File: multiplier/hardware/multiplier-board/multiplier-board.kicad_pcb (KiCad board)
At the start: 2 copper layers, 76.2 x 134.1 mm, 80 parts, among them U1 74AHCT08, U10 74HCT688, U11 74AHCT08, U12 74AHCT08, U13 74AHCT08, U14 74AHCT08, U15 74AHCT08, U16 74AHCT08, U17 74AHCT08, U18 74AHCT08, U19 ATF16V10C, U2 74AHCT08, U20 74AHCT374, U21 74LS283, U22 74LS283, U23 74LS283, U24 74LS283, U25 74LS283, U26 74LS283, U27 74LS283, U28 74AHCT374, U29 74LS283, U3 74AHCT08, U30 74LS283, U31 74LS283, U32 74LS283, U33 74LS283, U34 74LS283, U35 74LS283, U36 74AHCT245, U37 74AHCT245, U4 74AHCT08, U5 74AHCT08, U6 74AHCT08, U7 74AHCT08, U8 74AHCT08, U9 74HCT688

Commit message: corrected part designator
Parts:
- U21, U22, U23, U24, U25, U26, U27, U29, U30, U31, U32, U33, U34, U35: value 74LS283 -> 74HCT283
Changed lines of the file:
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@@
 			)
 		)
-		(property "Value" "74LS283"
+		(property "Value" "74HCT283"
 			(at 0 5.9 90)
 			(layer "F.Fab")
@@
 			)
 		)
-		(property "Value" "74LS283"
+		(property "Value" "74HCT283"
 			(at 0 5.9 90)
 			(layer "F.Fab")
@@
 			)
 		)
-		(property "Value" "74LS283"
+		(property "Value" "74HCT283"
 			(at 0 5.9 90)
 			(layer "F.Fab")
@@
 			)
 		)
-		(property "Value" "74LS283"
+		(property "Value" "74HCT283"
 			(at 0 5.9 90)
 			(layer "F.Fab")
@@
 			)
 		)
-		(property "Value" "74LS283"
+		(property "Value" "74HCT283"
 			(at 0 5.9 90)
 			(layer "F.Fab")
@@
 			)
 		)
-		(property "Value" "74LS283"
+		(property "Value" "74HCT283"
 			(at 0 5.9 90)
 			(layer "F.Fab")
@@
 			)
 		)
-		(property "Value" "74LS283"
+		(property "Value" "74HCT283"
 			(at 0 5.9 90)
 			(layer "F.Fab")
@@
 			)
 		)
-		(property "Value" "74LS283"
+		(property "Value" "74HCT283"
 			(at 0 5.9 90)
 			(layer "F.Fab")
@@
 			)
 		)
-		(property "Value" "74LS283"
+		(property "Value" "74HCT283"
 			(at 0 5.9 90)
 			(layer "F.Fab")
@@
 			)
 		)
-		(property "Value" "74LS283"
+		(property "Value" "74HCT283"
 			(at 0 5.9 90)
 			(layer "F.Fab")
@@
 			)
 		)
-		(property "Value" "74LS283"
+		(property "Value" "74HCT283"
 			(at 0 5.9 90)
 			(layer "F.Fab")
@@
 			)
 		)
-		(property "Value" "74LS283"
+		(property "Value" "74HCT283"
 			(at 0 5.9 90)
 			(layer "F.Fab")
@@
 			)
 		)
-		(property "Value" "74LS283"
+		(property "Value" "74HCT283"
 			(at 0 5.9 90)
 			(layer "F.Fab")
@@
 			)
 		)
-		(property "Value" "74LS283"
+		(property "Value" "74HCT283"
 			(at 0 5.9 90)
 			(layer "F.Fab")

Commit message: update kicad version
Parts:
- U19: value ATF16V10C -> ATF16V8C
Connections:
- net Net-(U19-I5) renamed /ADDR_HIGH
- net Net-(U20-Cp) renamed /AIN
- net Net-(U28-Cp) renamed /BIN
- net Net-(U36-CE) renamed /RHIGH
- net Net-(U37-CE) renamed /RLOW

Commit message: corrected issues
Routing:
- net CLK: track 27.7 -> 44.8 mm
- net GND: track 1248.2 -> 1235.3 mm
- net +5V: track 782.5 -> 791.8 mm
- net ~{RO}: track 62.0 -> 66.9 mm
- net /BUS4: track 100.3 -> 104.0 mm
- net /BUS6: track 93.5 -> 97.3 mm
- net /ADDR8: track 46.1 -> 49.7 mm
- net /ADDR10: track 34.2 -> 37.8 mm
- net /BUS2: track 108.2 -> 111.8 mm
- net /ADDR6: track 22.0 -> 25.5 mm
- net /BUS0: track 94.8 -> 98.4 mm
- net /ADDR4: track 20.9 -> 24.4 mm
- net /ADDR13: track 33.5 -> 30.0 mm
- net /ADDR15: track 34.2 -> 30.7 mm
- net /ADDR1: track 23.7 -> 20.2 mm
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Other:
- board text added: "v1.1 by Michael Kanmprath"
- board text removed: "v1.0 by Michael Kanmprath"

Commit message: changed pcb to 4-layer with internal ground planes
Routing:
- net GND: track 1235.3 -> 1241.5 mm
- added copper zone on In1.Cu, net GND
- added copper zone on In2.Cu, net GND
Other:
- copper layers 2 -> 4
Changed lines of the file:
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@@
 	(layers
 		(0 "F.Cu" signal)
+		(4 "In1.Cu" signal)
+		(6 "In2.Cu" signal)
 		(2 "B.Cu" signal)
 		(9 "F.Adhes" user "F.Adhesive")
@@
 	)
 	(setup
+		(stackup
+			(layer "F.SilkS"
+				(type "Top Silk Screen")
+			)
+			(layer "F.Paste"
+				(type "Top Solder Paste")
+			)
+			(layer "F.Mask"
+				(type "Top Solder Mask")
+				(thickness 0.01)
+			)
+			(layer "F.Cu"
+				(type "copper")
+				(thickness 0.035)
+			)
+			(layer "dielectric 1"
+				(type "prepreg")
+				(thickness 0.1)
+				(material "FR4")
+				(epsilon_r 4.5)
+				(loss_tangent 0.02)
+			)
+			(layer "In1.Cu"
+				(type "copper")
+				(thickness 0.035)
+			)
+			(layer "dielectric 2"
+				(type "core")
+				(thickness 1.24)
+				(material "FR4")
+				(epsilon_r 4.5)
+				(loss_tangent 0.02)
+			)
+			(layer "In2.Cu"
+				(type "copper")
+				(thickness 0.035)
+			)
+			(layer "dielectric 3"
+				(type "prepreg")
+				(thickness 0.1)
+				(material "FR4")
+				(epsilon_r 4.5)
+				(loss_tangent 0.02)
+			)
+			(layer "B.Cu"
+				(type "copper")
+				(thickness 0.035)
+			)
+			(layer "B.Mask"
+				(type "Bottom Solder Mask")
+				(thickness 0.01)
+			)
+			(layer "B.Paste"
+				(type "Bottom Solder Paste")
+			)
+			(layer "B.SilkS"
+				(type "Bottom Silk Screen")
+			)
+			(copper_finish "None")
+			(dielectric_constraints no)
+		)
 		(pad_to_mask_clearance 0)
 		(allow_soldermask_bridges_in_footprints no)
@@
 	)
 	(segment
+		(start 106.9 147.56)
+		(end 106.9 147.4)
+		(width 0.75)
+		(layer "In1.Cu")
+		(net 2)
+	)
+	(segment
+		(start 106.9 147.4)
+		(end 105 145.5)
+		(width 0.75)
+		(layer "In1.Cu")
+		(net 2)
+	)
+	(segment
+		(start 106.9 147.56)
+		(end 105 145.66)
+		(width 0.75)
+		(layer "In2.Cu")
+		(net 2)
+	)
+	(segment
+		(start 105 145.66)
+		(end 105 145)
+		(width 0.75)
+		(layer "In2.Cu")
+		(net 2)
+	)
+	(segment
 		(start 110.824 144.769169)
 		(end 110.824 146.404)
@@
 		(net 2)
 		(net_name "GND")
-		(layer "B.Cu")
+		(layers "B.Cu" "In1.Cu" "In2.Cu")
 		(hatch edge 0.5)
 		(connect_pads

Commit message: improved signal line isolation
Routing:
- net /AIN: track 47.8 -> 54.1 mm
- net /BIN: track 50.6 -> 52.8 mm
- net GND: track 1241.5 -> 1239.7 mm
- net /RLOW: track 63.6 -> 62.6 mm, vias 1 -> 2
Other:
- board text added: "v1.2 by Michael Kanmprath"
- board text removed: "v1.1 by Michael Kanmprath"
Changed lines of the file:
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@@
 		(layer "Edge.Cuts")
 	)
-	(gr_text "v1.1 by Michael Kanmprath"
+	(gr_text "v1.2 by Michael Kanmprath"
 		(at 159.131 19.6342 270)
 		(layer "F.SilkS")
@@
 	)
 	(segment
+		(start 91.868 98.0694)
+		(end 91.868 93.6752)
+		(width 0.75)
+		(layer "B.Cu")
+		(net 2)
+	)
+	(segment
 		(start 152.146 137.6934)
 		(end 158.0134 137.6934)
@@
 	)
 	(segment
-		(start 91.8718 98.024348)
-		(end 96.220948 93.6752)
-		(width 0.75)
-		(layer "B.Cu")
-		(net 2)
-	)
-	(segment
 		(start 146.9644 142.875)
 		(end 152.146 137.6934)
@@
 	)
 	(segment
-		(start 96.220948 93.6752)
-		(end 125.984 93.6752)
-		(width 0.75)
-		(layer "B.Cu")
-		(net 2)
-	)
-	(segment
 		(start 103.632 18.796)
 		(end 104.775 19.939)
@@
 	)
 	(segment
-		(start 91.868 98.0694)
+		(start 91.868 93.6752)
 		(end 91.868 20.5415)
 		(width 0.75)
@@
 	)
 	(segment
-		(start 125.984 93.6752)
-		(end 128.4732 96.1644)
-		(width 0.75)
-		(layer "B.Cu")
-		(net 2)
-	)
-	(segment
 		(start 122.301 18.796)
 		(end 138.049 18.796)
@@
 	)
 	(segment
+		(start 128.4732 96.1644)
+		(end 125.984 93.6752)
+		(width 0.75)
+		(layer "B.Cu")
+		(net 2)
+	)
+	(segment
 		(start 118.6688 129.3915)
 		(end 121.7129 129.3915)
@@
 	)
 	(segment
+		(start 125.984 93.6752)
+		(end 91.868 93.6752)
+		(width 0.75)
+		(layer "B.Cu")
+		(net 2)
+	)
+	(segment
 		(start 104.902 20.066)
 		(end 105.156 20.32)
@@
 	)
 	(segment
-		(start 95.3262 102.8954)
-		(end 95.3262 95.8596)
+		(start 107.823 123.9012)
+		(end 107.2642 123.3424)
 		(width 0.2)
 		(layer "B.Cu")
@@
 	)
 	(segment
-		(start 100.4824 108.0516)
-		(end 95.3262 102.8954)
+		(start 107.2642 111.2012)
+		(end 105.0544 108.9914)
 		(width 0.2)
 		(layer "B.Cu")
@@
 	)
 	(segment
-		(start 95.3262 95.8596)
-		(end 95.3008 95.8342)
+		(start 116.1288 123.3932)
+		(end 115.6208 123.9012)
 		(width 0.2)
 		(layer "B.Cu")
@@
 	)
 	(segment
-		(start 105.41 108.0516)
-		(end 100.4824 108.0516)
+		(start 105.0544 108.9914)
+		(end 94.2848 108.9914)
 		(width 0.2)
 		(layer "B.Cu")
@@
 	)
 	(segment
-		(start 107.2388 122.936)
-		(end 107.2388 109.8804)
+		(start 116.1288 121.7715)
+		(end 116.1288 123.3932)
 		(width 0.2)
 		(layer "B.Cu")
@@
 	)
 	(segment
-		(start 108.6358 124.333)
-		(end 107.2388 122.936)
+		(start 92.964 107.6706)
+		(end 92.964 96.5454)
 		(width 0.2)
 		(layer "B.Cu")
@@
 	)
 	(segment
-		(start 107.2388 109.8804)
-		(end 105.41 108.0516)
+		(start 92.964 96.5454)
+		(end 93.6752 95.8342)
 		(width 0.2)
 		(layer "B.Cu")
@@
 	)
 	(segment
-		(start 116.1288 121.7715)
-		(end 116.1288 123.1646)
+		(start 115.6208 123.9012)
+		(end 107.823 123.9012)
+		(width 0.2)
+		(layer "B.Cu")
+		(net 112)
+	)
+	(segment
+		(start 94.2848 108.9914)
+		(end 92.964 107.6706)
+		(width 0.2)
+		(layer "B.Cu")
+		(net 112)
+	)
+	(segment
+		(start 107.2642 123.3424)
+		(end 107.2642 111.2012)
 		(width 0.2)
 		(layer "B.Cu")
@@
 	)
 	(segment
-		(start 116.1288 123.1646)
-		(end 114.9604 124.333)
+		(start 95.3262 95.8596)
+		(end 95.3008 95.8342)
 		(width 0.2)
 		(layer "B.Cu")
@@
 	)
 	(segment
-		(start 114.9604 124.333)
-		(end 108.6358 124.333)
+		(start 93.6752 95.8342)
+		(end 95.3008 95.8342)
 		(width 0.2)
 		(layer "B.Cu")
@@
 	)
 	(segment
+		(start 108.5088 121.7715)
+		(end 114.9643 115.316)
+		(width 0.2)
+		(layer "F.Cu")
+		(net 129)
+	)
+	(segment
 		(start 149.4282 104.6984)
 		(end 149.4282 115.7986)
@@
 		(net 129)
 	)
-	(via
-		(at 149.4282 115.7986)
-		(size 0.6)
-		(drill 0.3)
-		(layers "F.Cu" "B.Cu")
-		(net 129)
-	)
 	(segment
-		(start 108.5088 121.7715)
-		(end 108.5088 123.0938)
+		(start 114.9643 115.316)
+		(end 114.9858 115.316)
 		(width 0.2)
-		(layer "B.Cu")
+		(layer "F.Cu")
 		(net 129)
 	)
-	(segment
-		(start 146.832 118.4202)
-		(end 149.4282 115.824)
-		(width 0.2)
-		(layer "B.Cu")
+	(via
+		(at 114.9858 115.316)
+		(size 0.6)
+		(drill 0.3)
+		(layers "F.Cu" "B.Cu")
 		(net 129)
 	)
-	(segment
-		(start 114.8588 123.2716)
-		(end 114.8588 121.48445)
-		(width 0.2)
-		(layer "B.Cu")
+	(via
+		(at 149.4282 115.7986)
+		(size 0.6)
+		(drill 0.3)
+		(layers "F.Cu" "B.Cu")
 		(net 129)
 	)
 	(segment
-		(start 108.5088 123.0938)
-		(end 109.347 123.932)
+		(start 114.9858 115.316)
+		(end 118.09 118.4202)
 		(width 0.2)
 		(layer "B.Cu")
@@
 	)
 	(segment
-		(start 117.92305 118.4202)
+		(start 118.4656 118.4202)
 		(end 146.832 118.4202)
 		(width 0.2)
@@
 	)
 	(segment
-		(start 109.347 123.932)
-		(end 114.1984 123.932)
-		(width 0.2)
-		(layer "B.Cu")
-		(net 129)
-	)
-	(segment
-		(start 114.8588 121.48445)
-		(end 117.92305 118.4202)
+		(start 146.832 118.4202)
+		(end 149.4282 115.824)
 		(width 0.2)
 		(layer "B.Cu")
@@
 	)
 	(segment
-		(start 114.1984 123.932)
-		(end 114.8588 123.2716)
+		(start 118.09 118.4202)
+		(end 118.4656 118.4202)
 		(width 0.2)
 		(layer "B.Cu")
@@
 	)
 	(segment
-		(start 113.5888 119.5378)
-		(end 113.5888 115.6633)
+		(start 96.3422 106.68)
+		(end 96.3422 99.4156)
 		(width 0.2)
 		(layer "B.Cu")
@@
 	)
 	(segment
-		(start 113.5888 121.7715)
-		(end 113.5888 119.5378)
+		(start 96.3422 99.4156)
+		(end 100.3554 95.4024)
 		(width 0.2)
 		(layer "B.Cu")
@@
 	)
 	(segment
-		(start 100.0452 95.4024)
-		(end 110.3376 95.4024)
+		(start 113.5888 114.0968)
+		(end 106.7816 107.2896)
 		(width 0.2)
 		(layer "B.Cu")
@@
 	)
 	(segment
-		(start 100.6485 107.6506)
-		(end 95.7272 102.7293)
-		(width 0.2)
-		(layer "B.Cu")
-		(net 160)
-	)
-	(segment
-		(start 95.7272 99.7204)
-		(end 100.0452 95.4024)
+		(start 100.3554 95.4024)
+		(end 110.3376 95.4024)
 		(width 0.2)
 		(layer "B.Cu")
@@
 	)
 	(segment
-		(start 105.5761 107.6506)
-		(end 100.6485 107.6506)
+		(start 113.5888 121.7715)
+		(end 113.5888 114.0968)
 		(width 0.2)
 		(layer "B.Cu")
@@
 	)
 	(segment
-		(start 113.5888 115.6633)
-		(end 105.5761 107.6506)
+		(start 106.7816 107.2896)
+		(end 96.9518 107.2896)
 		(width 0.2)
 		(layer "B.Cu")
@@
 	)
 	(segment
-		(start 95.7272 102.7293)
-		(end 95.7272 99.7204)
+		(start 96.9518 107.2896)
+		(end 96.3422 106.68)
 		(width 0.2)
 		(layer "B.Cu")

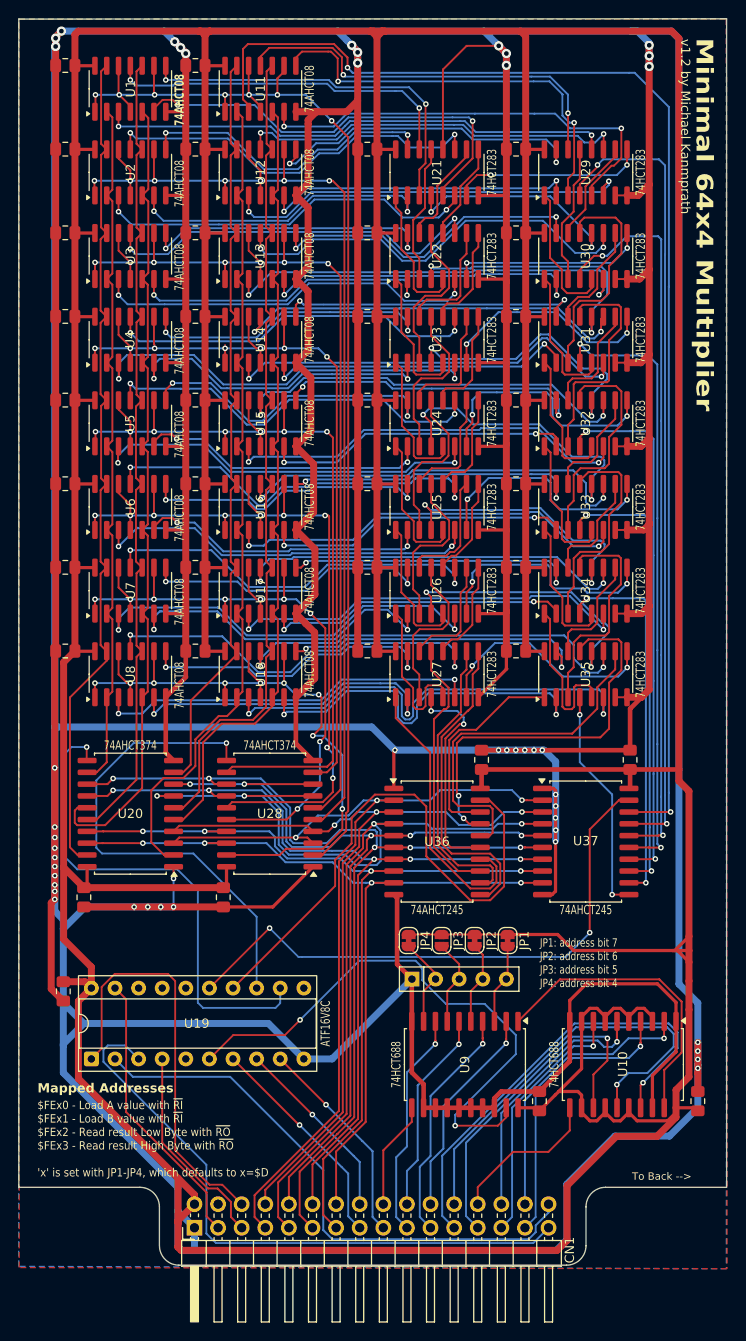
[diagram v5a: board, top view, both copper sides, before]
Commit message: improved signal integrity
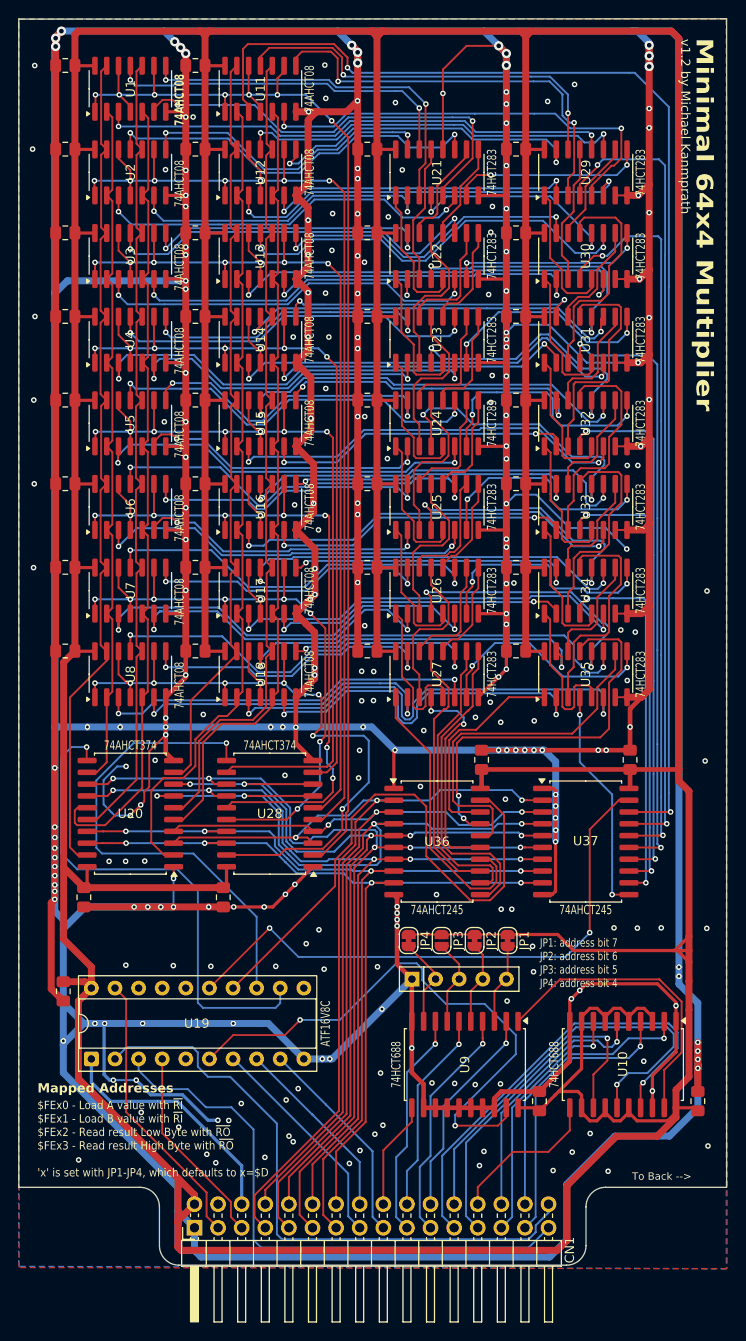
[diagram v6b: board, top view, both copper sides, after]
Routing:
- net GND: track 1239.7 -> 1319.9 mm, vias 46 -> 267
- net CLK: track 44.8 -> 26.5 mm
- net ~{RO}: track 66.9 -> 61.1 mm
- net ~{RI}: track 61.0 -> 66.1 mm
- net B7: track 76.3 -> 81.2 mm
- net ~{RST}: track 22.3 -> 21.7 mm
- net /ADDR2: vias 1 -> 0
- net /ADDR1: vias 1 -> 0
- net /ADDR0: vias 1 -> 0
- added copper zone on F.Cu, net GND
- removed copper zone on F.Cu, net +5V
- removed copper zone on In1.Cu, net GND
- removed copper zone on In2.Cu, net GND
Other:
- copper layers 4 -> 2
